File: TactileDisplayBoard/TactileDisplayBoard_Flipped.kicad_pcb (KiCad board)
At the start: 2 copper layers, 87 x 67 mm, 12 parts, among them J1 Conn_01x02, J2 Conn_01x02, J3 Microstep_Jumper, J4 Conn_Motor, J5 Microstep_Jumper, J6 Conn_Motor, J7 PowerSwitch, U1 A4988, U2 ESP32-DEVKITC, U3 A4988

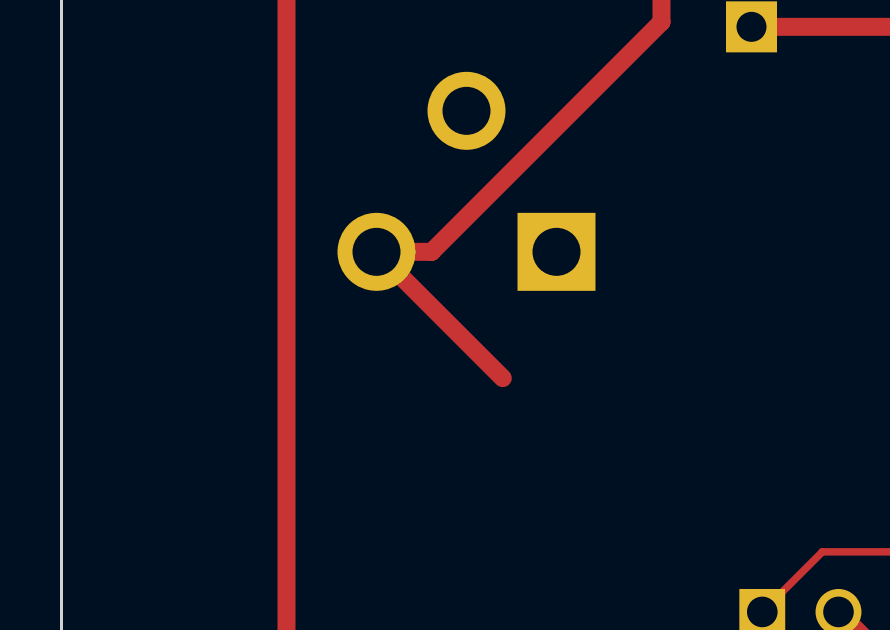
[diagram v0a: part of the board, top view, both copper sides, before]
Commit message: Removed Legacy Trace
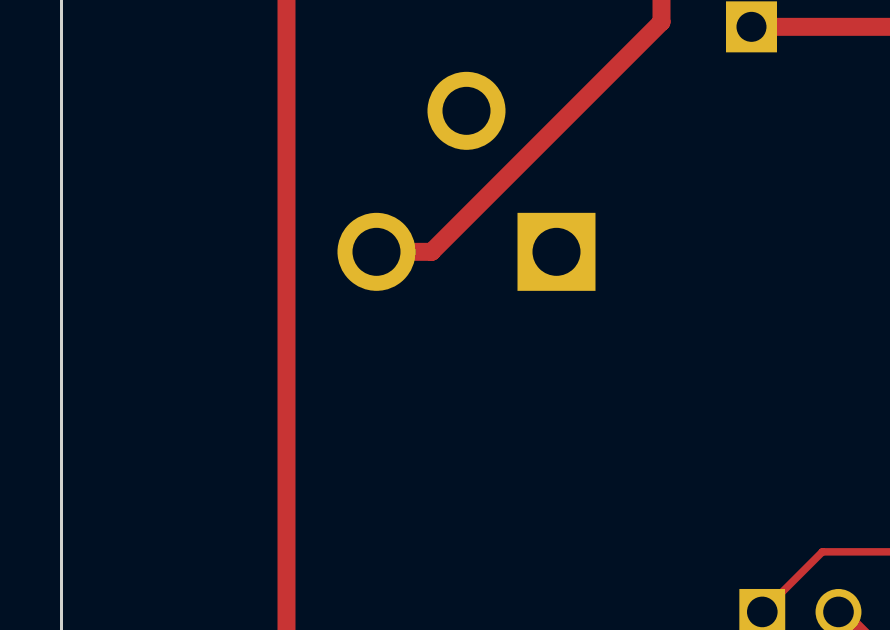
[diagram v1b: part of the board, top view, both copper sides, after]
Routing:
- net +5V: track 242.3 -> 236.4 mm
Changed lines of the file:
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@@
   (segment (start 94.5 49.5) (end 94.5 80) (width 0.6) (layer "F.Cu") (net 1))
   (segment (start 169.85 43.28) (end 167.87 41.3) (width 0.6) (layer "F.Cu") (net 3))
-  (segment (start 112 39.5) (end 166.07 39.5) (width 0.6) (layer "F.Cu") (net 3))
+  (segment (start 107 52.838477) (end 107 44.5) (width 0.6) (layer "F.Cu") (net 3))
   (segment (start 156.35 84.35) (end 156.35 85.35) (width 0.6) (layer "F.Cu") (net 3))
-  (segment (start 107 52.838477) (end 107 44.5) (width 0.6) (layer "F.Cu") (net 3))
   (segment (start 136.29 81.525) (end 138.265 83.5) (width 0.6) (layer "F.Cu") (net 3))
   (segment (start 156.35 85.35) (end 159 88) (width 0.6) (layer "F.Cu") (net 3))
   (segment (start 169 76.0925) (end 169.85 75.2425) (width 0.6) (layer "F.Cu") (net 3))
   (segment (start 162.1725 88) (end 169 81.1725) (width 0.6) (layer "F.Cu") (net 3))
+  (segment (start 107 44.5) (end 112 39.5) (width 0.6) (layer "F.Cu") (net 3))
+  (segment (start 138.5 102.5) (end 125.6 89.6) (width 0.6) (layer "F.Cu") (net 3))
   (segment (start 166.07 39.5) (end 167.87 41.3) (width 0.6) (layer "F.Cu") (net 3))
-  (segment (start 138.5 102.5) (end 125.6 89.6) (width 0.6) (layer "F.Cu") (net 3))
-  (segment (start 107 44.5) (end 112 39.5) (width 0.6) (layer "F.Cu") (net 3))
   (segment (start 155.81749 102.5) (end 138.5 102.5) (width 0.6) (layer "F.Cu") (net 3))
   (segment (start 155.5 83.5) (end 156.35 84.35) (width 0.6) (layer "F.Cu") (net 3))
+  (segment (start 112 39.5) (end 166.07 39.5) (width 0.6) (layer "F.Cu") (net 3))
   (segment (start 125.6 89.6) (end 125.6 85.2025) (width 0.6) (layer "F.Cu") (net 3))
   (segment (start 169 89.31749) (end 155.81749 102.5) (width 0.6) (layer "F.Cu") (net 3))
@@
   (segment (start 169 78.6325) (end 169 81.1725) (width 0.6) (layer "F.Cu") (net 3))
   (segment (start 169 81.1725) (end 169 89.31749) (width 0.6) (layer "F.Cu") (net 3))
+  (segment (start 169.85 75.2425) (end 169.85 43.28) (width 0.6) (layer "F.Cu") (net 3))
+  (segment (start 97.5 60.5) (end 99.338477 60.5) (width 0.6) (layer "F.Cu") (net 3))
   (segment (start 99.338477 60.5) (end 107 52.838477) (width 0.6) (layer "F.Cu") (net 3))
-  (segment (start 169.85 75.2425) (end 169.85 43.28) (width 0.6) (layer "F.Cu") (net 3))
   (segment (start 136.29 81.525) (end 136.29 78.985) (width 0.6) (layer "F.Cu") (net 3))
-  (segment (start 101.71 64.71) (end 97.5 60.5) (width 0.6) (layer "F.Cu") (net 3))
-  (segment (start 97.5 60.5) (end 99.338477 60.5) (width 0.6) (layer "F.Cu") (net 3))
   (segment (start 118 100) (end 118 84.87) (width 0.8) (layer "F.Cu") (net 4))
   (segment (start 115.44 99.94) (end 115.5 100) (width 0.8) (layer "F.Cu") (net 5))
